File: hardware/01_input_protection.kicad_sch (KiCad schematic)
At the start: 22 parts, among them J1 USB4105-GF-A, Q1 MMBT3906, U1 CH224K, U2 TPS26600PWPR

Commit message: Update on the PCB.
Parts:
- U1: value CH224K -> CH224A

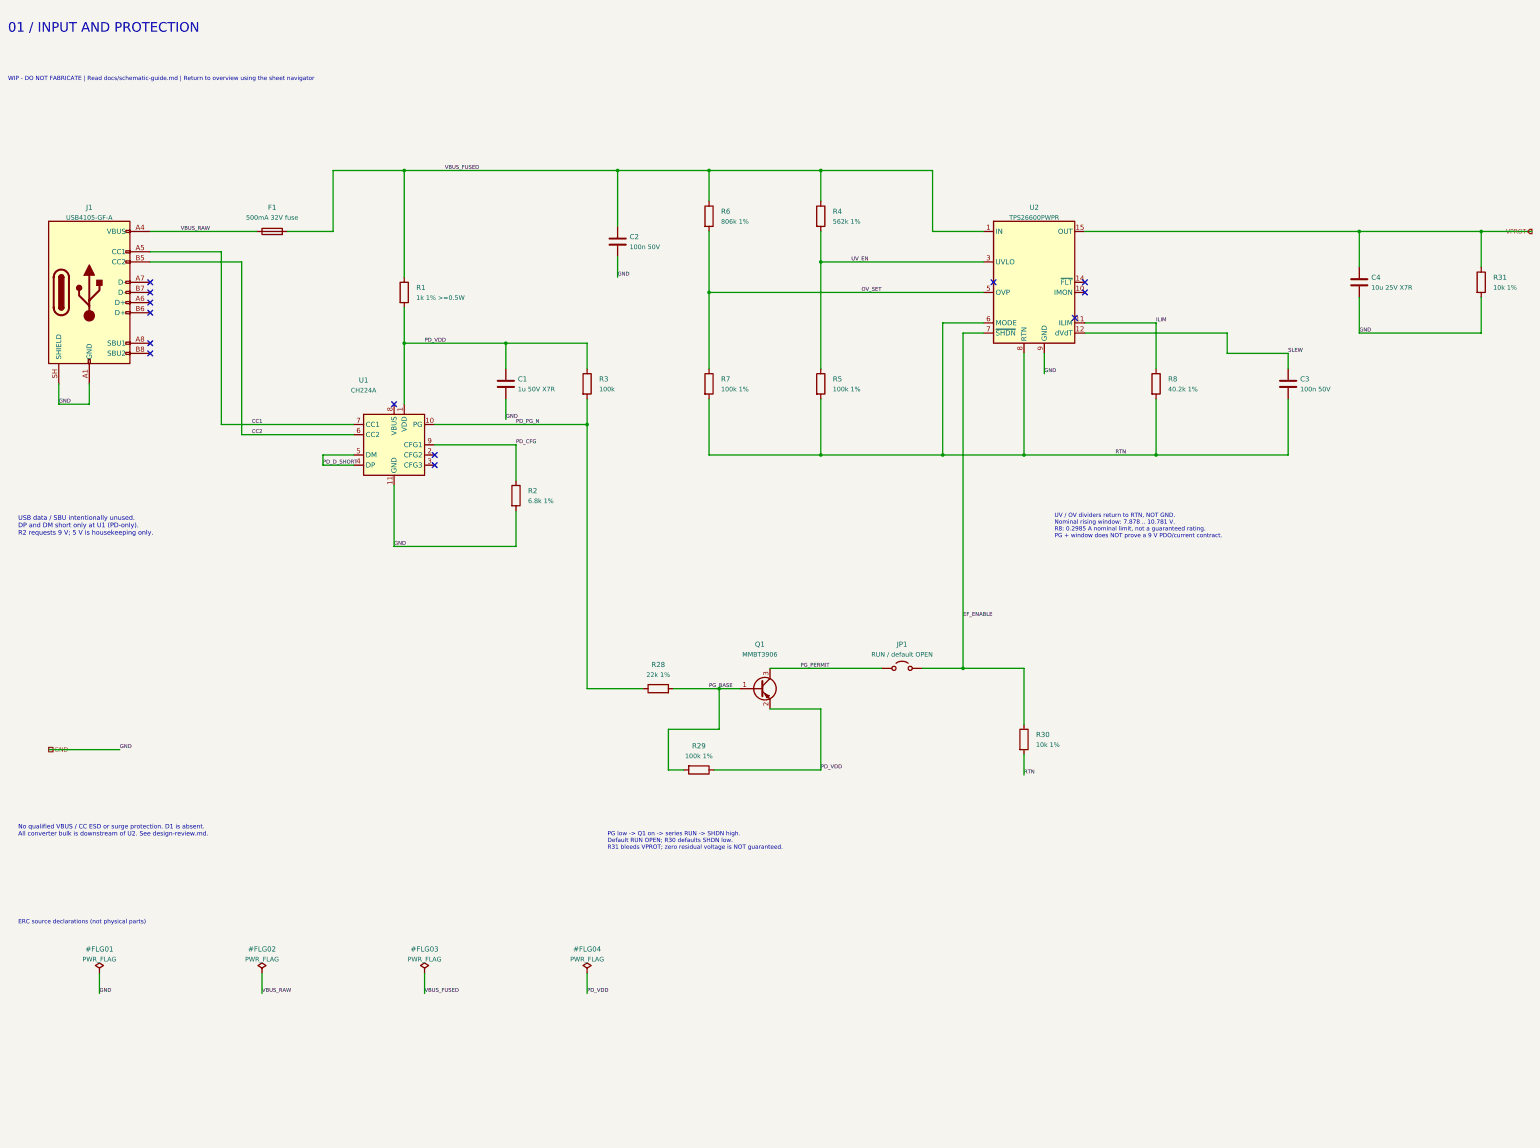
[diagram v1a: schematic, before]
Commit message: Save 9 V power-supply schematic prototype and LED mechanical provisions
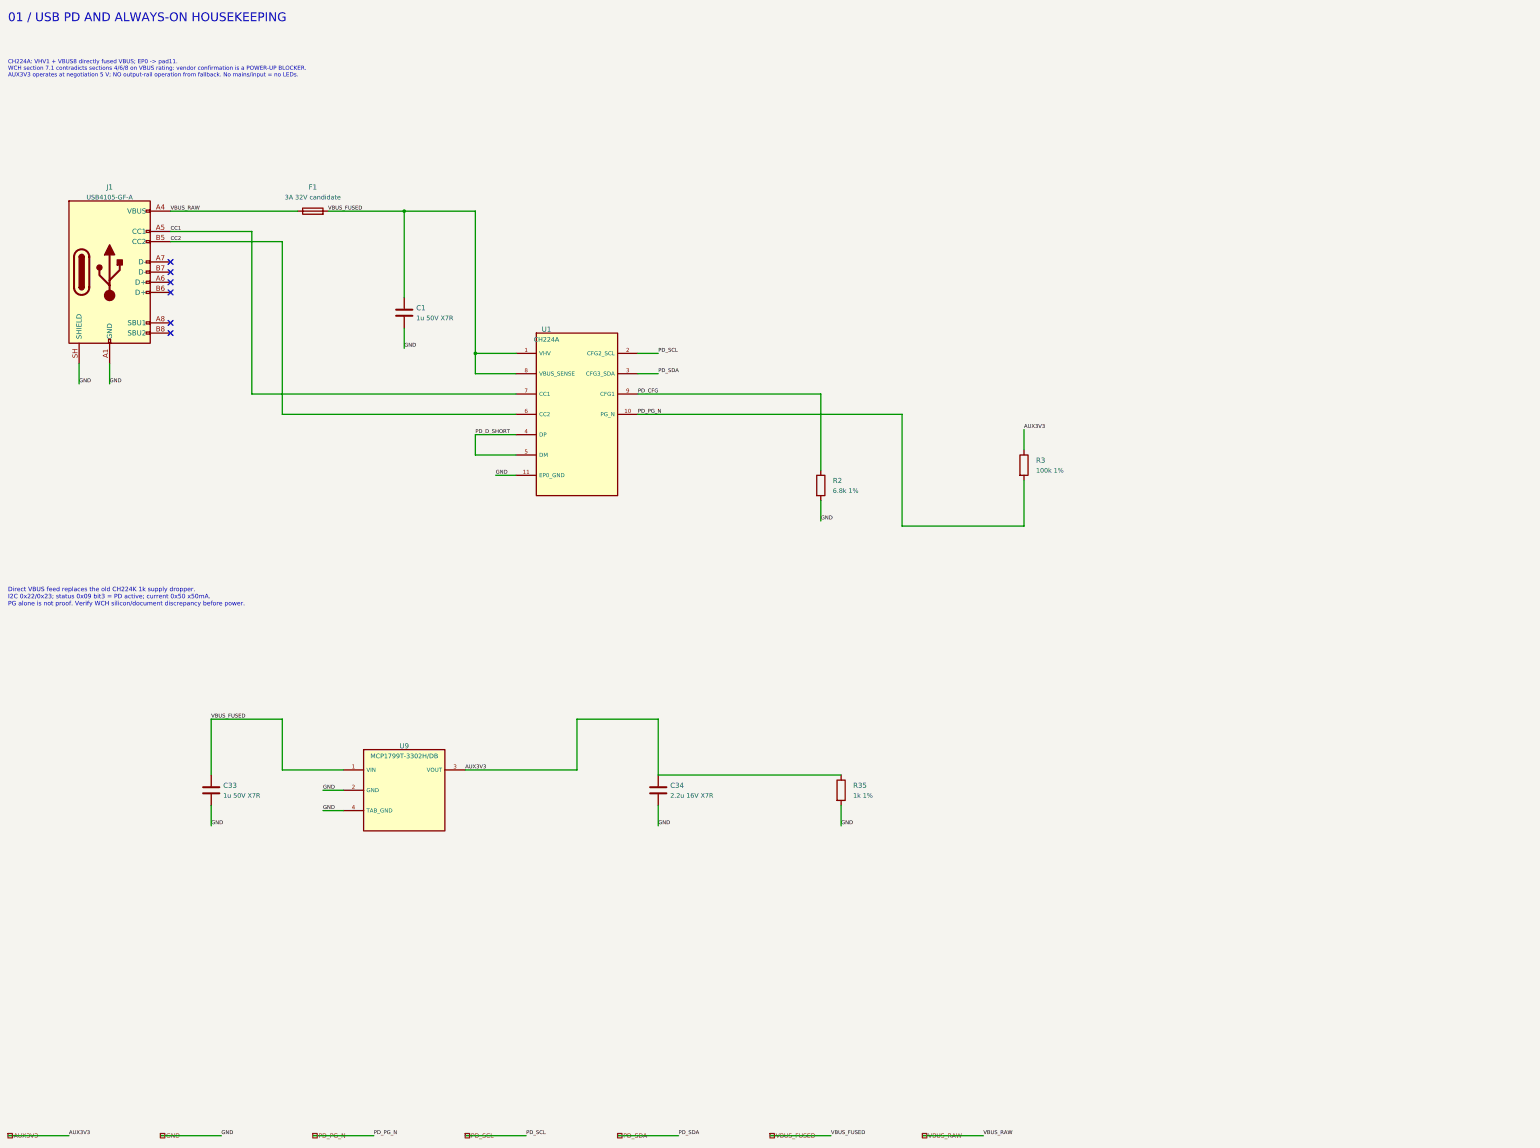
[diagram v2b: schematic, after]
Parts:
- removed C2, C3: 100n 50V, Capacitor_SMD:C_1206_3216Metric, symbol BigModular:Device_C
- removed C4: 10u 25V X7R, Capacitor_SMD:C_1206_3216Metric, symbol BigModular:Device_C
- removed JP1: RUN / default OPEN, symbol BigModular:Jumper_Jumper_2_Open
- removed Q1: MMBT3906, Package_TO_SOT_SMD:SOT-23, symbol BigModular:Transistor_BJT_MMBT3906
- removed R1: 1k 1% >=0.5W, Resistor_SMD:R_2010_5025Metric, symbol BigModular:Device_R
- removed R28: 22k 1%, Resistor_SMD:R_0603_1608Metric, symbol BigModular:Device_R
- removed R29, R5, R7: 100k 1%, Resistor_SMD:R_0603_1608Metric, symbol BigModular:Device_R
- removed R30, R31: 10k 1%, Resistor_SMD:R_0603_1608Metric, symbol BigModular:Device_R
- removed R4: 562k 1%, Resistor_SMD:R_0603_1608Metric, symbol BigModular:Device_R
- removed R6: 806k 1%, Resistor_SMD:R_0603_1608Metric, symbol BigModular:Device_R
- removed R8: 40.2k 1%, Resistor_SMD:R_0603_1608Metric, symbol BigModular:Device_R
- removed U2: TPS26600PWPR, Package_SO:HTSSOP-16-1EP_4.4x5mm_P0.65mm_EP3.4x5mm_Mask2.66x2.46mm_ThermalVias, symbol BigModular:Power_Management_TPS26600PWP
- added C33: 1u 50V X7R, BigModular:C_0805_2012Metric, symbol BigModular:Device_C
- added C34: 2.2u 16V X7R, BigModular:C_0805_2012Metric, symbol BigModular:Device_C
- added R35: 1k 1%, BigModular:R_0603_1608Metric, symbol BigModular:Device_R
- added U9: MCP1799T-3302H/DB, BigModular:MCP1799_SOT223_Tab4, symbol BigModular:MCP1799T_3302H_DB
- C1: footprint Capacitor_SMD:C_1206_3216Metric -> BigModular:C_0805_2012Metric; JLCPCB Audit Requirements (none) -> {}; JLCPCB Exclude (none) -> no; NOTE (none) -> Effective capacitance under DC bias and temperature must be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
- F1: value 500mA 32V fuse -> 3A 32V candidate; footprint (none) -> BigModular:Fuse_1206_3216Metric; JLCPCB Audit Requirements (none) -> {}; JLCPCB Exclude (none) -> no; LCSC (none) -> C14165; MPN (none) -> 0466003.NRHF; NOTE Unselected candidate: 32V rating covers steady 20/21V only;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 -> 0466003.NRHF catalog candidate only; source/fuse/eFuse ther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
- J1: JLCPCB Audit Requirements (none) -> {"assembly": "manual", "reason": "User-selected manual inte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; JLCPCB Exclude (none) -> yes; NOTE Only electrical footprint placed. Drawing Rev B: axis 1.73 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 -> Prototype candidate; qualify ratings, land pattern and oper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
- R2: footprint Resistor_SMD:R_0603_1608Metric -> BigModular:R_0603_1608Metric; JLCPCB Audit Requirements (none) -> {}; JLCPCB Exclude (none) -> no; LCSC (none) -> C23212; MPN (none) -> 0603WAF6801T5E; NOTE (none) -> Prototype candidate; qualify ratings, land pattern and oper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
- R3: value 100k -> 100k 1%; footprint Resistor_SMD:R_0603_1608Metric -> BigModular:R_0603_1608Metric; JLCPCB Audit Requirements (none) -> {}; JLCPCB Exclude (none) -> no; LCSC (none) -> C25803; MPN (none) -> 0603WAF1003T5E; NOTE (none) -> Prototype candidate; qualify ratings, land pattern and oper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
- U1: footprint Package_SO:SSOP-10-1EP_3.9x4.9mm_P1mm_EP2.1x3.3mm -> BigModular:SSOP-10-1EP_3.9x4.9mm_P1mm_EP2.1x3.3mm; symbol BigModular:Interface_USB_CH224K -> BigModular:CH224A; JLCPCB Audit Requirements (none) -> {}; JLCPCB Exclude (none) -> no; LCSC C970725 -> C42459160; MPN CH224K -> CH224A; NOTE WCH v1F fig6.1/6.3; datasheet EP0 maps to library pad11. DP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 -> WCH V2 table4-1; VHV1 is high-voltage input. EP0 mapped to 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
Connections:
- net GND: now also C33.2, C34.2, R35.2, U9.2 (GND), U9.4 (TAB_GND)
- net VBUS_FUSED: now also C1.1, U1.1 (VHV), U1.8 (VBUS_SENSE), C33.1, U9.1 (VIN)
- net PD_SCL: now reaches U1.2 (CFG2_SCL)
- net PD_SDA: now reaches U1.3 (CFG3_SDA)
- removed net PD_VDD: C1.1, R3.1, U1.1 (VDD)
- new net AUX3V3: C34.1, R3.1, R35.1, U9.3 (VOUT)
- no-connect marks 13 -> 6
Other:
- note added: "01 / USB PD AND ALWAYS-ON HOUSEKEEPING"
- note added: "CH224A: VHV1 + VBUS8 directly fused VBUS; EP0 -> pad11. WCH section 7.1 contradicts sections 4/6/8 on VBUS rating: vendor confirmation is a POWER-UP BLOCKER. AUX3V3 operates at negotiation 5 V; NO output-rail operation from fallback. No mains/input = no LEDs."
- note added: "Direct VBUS feed replaces the old CH224K 1k supply dropper. I2C 0x22/0x23; status 0x09 bit3 = PD active; current 0x50 x50mA. PG alone is not proof. Verify WCH silicon/document discrepancy before power."
- note removed: "01 / INPUT AND PROTECTION"
- note removed: "ERC source declarations (not physical parts)"
- note removed: "No qualified VBUS / CC ESD or surge protection. D1 is absent. All converter bulk is downstream of U2. See design-review.md."
- note removed: "PG low -> Q1 on -> series RUN -> SHDN high. Default RUN OPEN; R30 defaults SHDN low. R31 bleeds VPROT; zero residual voltage is NOT guaranteed."
- note removed: "USB data / SBU intentionally unused. DP and DM short only at U1 (PD-only). R2 requests 9 V; 5 V is housekeeping only."
- note removed: "UV / OV dividers return to RTN, NOT GND. Nominal rising window: 7.878 .. 10.781 V. R8: 0.2985 A nominal limit, not a guaranteed rating. PG + window does NOT prove a 9 V PDO/current contract."
- note removed: "WIP - DO NOT FABRICATE | Read docs/schematic-guide.md | Return to overview using the sheet navigator"
- title: Big Modular - Input and protection -> Big Modular - USB PD and always-on housekeeping
- moved on the sheet: C1, F1, J1, R2, R3, U1

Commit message: Clarify hierarchical ports and replace local label islands with visible schematic wiring
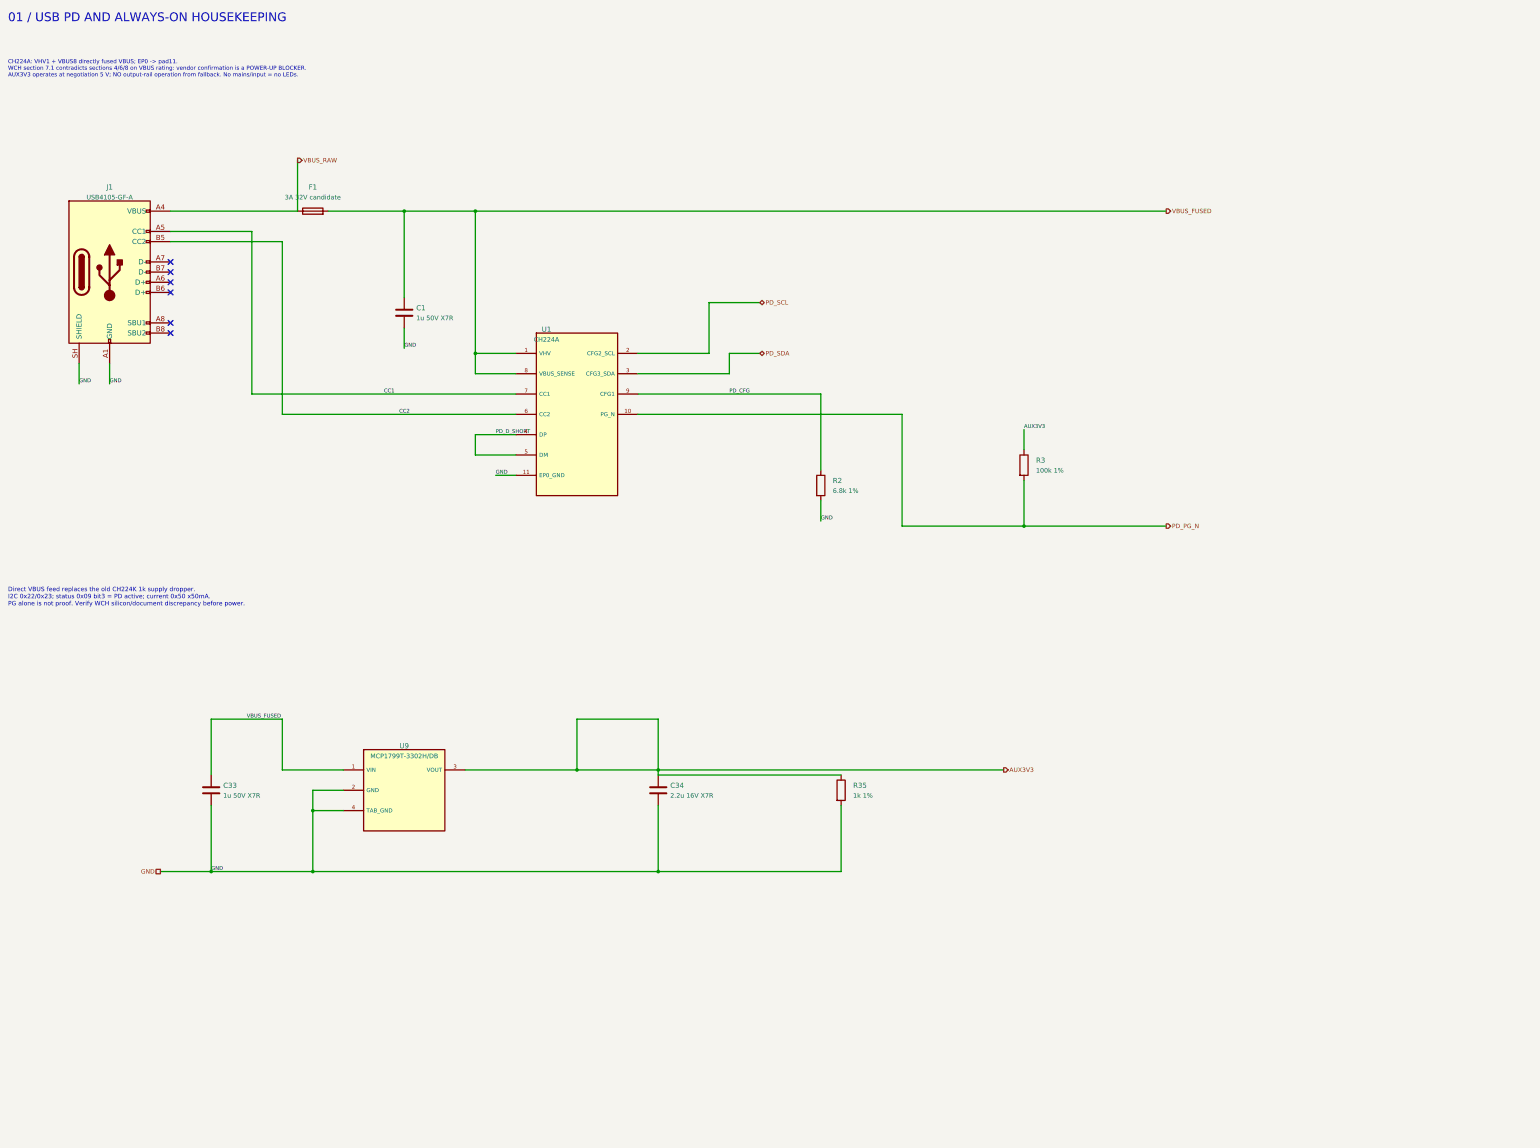
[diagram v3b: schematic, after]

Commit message: Simplify V1 power architecture, remove auxiliary sensing and obsolete documentation, enable autonomous protected start and reset button
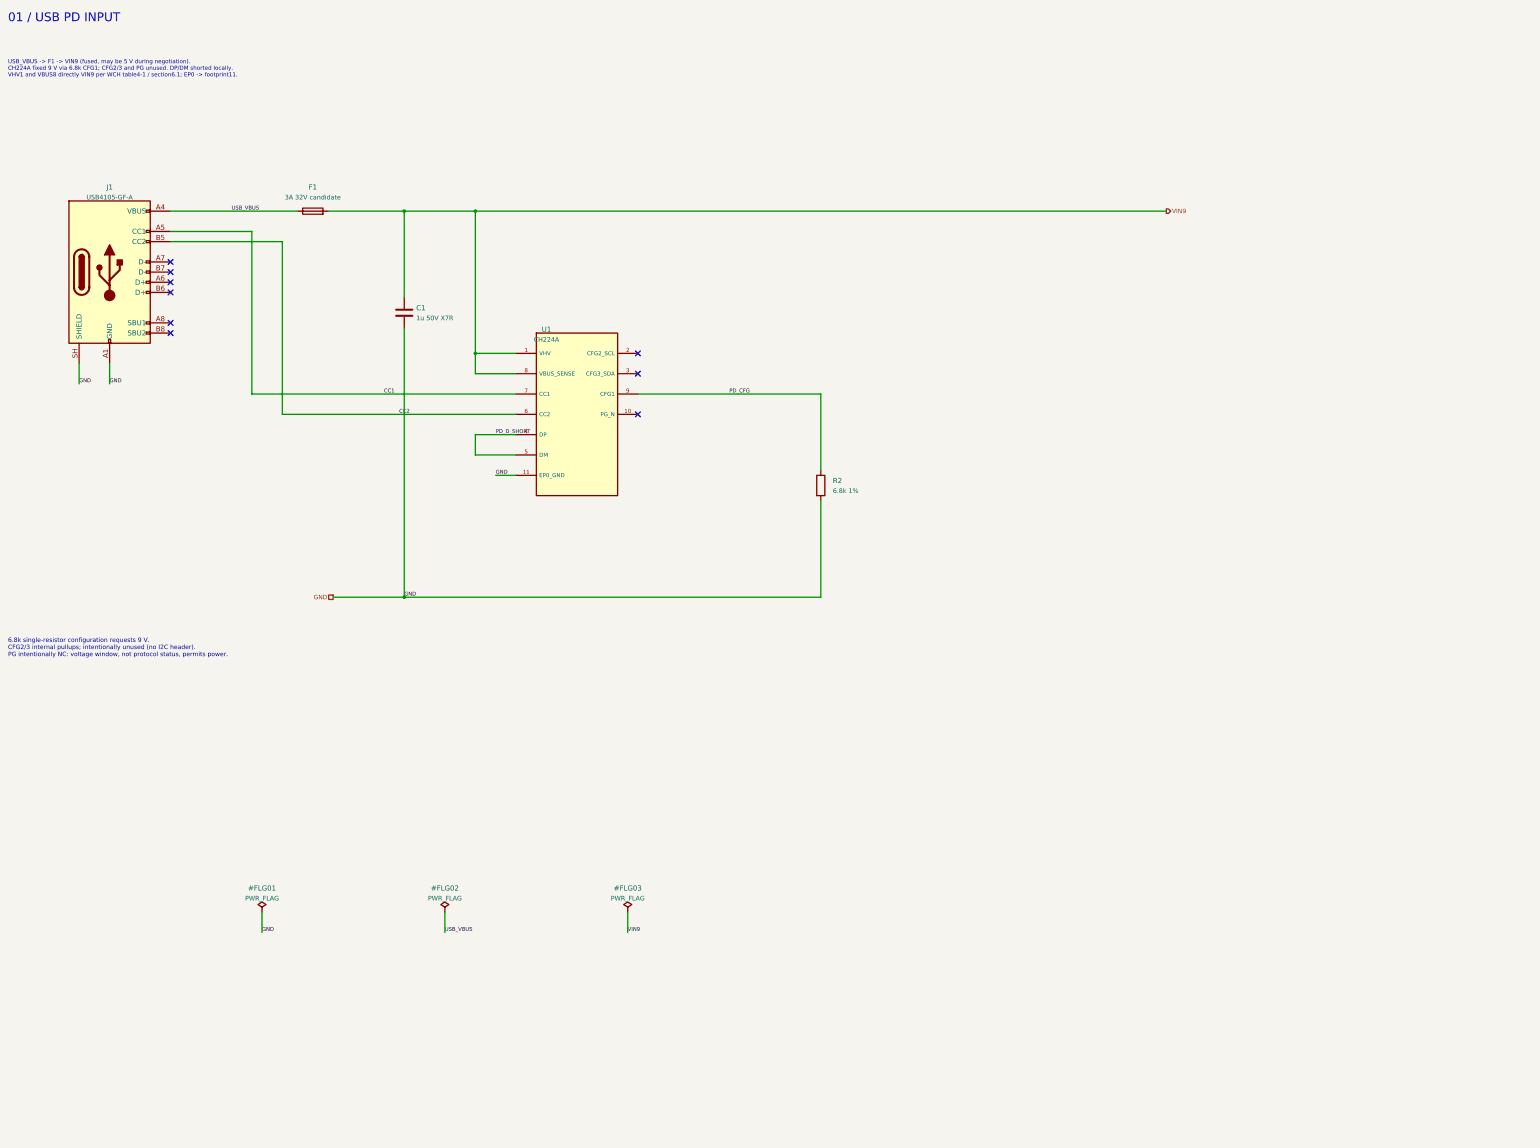
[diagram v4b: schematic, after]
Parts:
- removed C33: 1u 50V X7R, BigModular:C_0805_2012Metric, symbol BigModular:Device_C
- removed C34: 2.2u 16V X7R, BigModular:C_0805_2012Metric, symbol BigModular:Device_C
- removed R3: 100k 1%, BigModular:R_0603_1608Metric, symbol BigModular:Device_R
- removed R35: 1k 1%, BigModular:R_0603_1608Metric, symbol BigModular:Device_R
- removed U9: MCP1799T-3302H/DB, BigModular:MCP1799_SOT223_Tab4, symbol BigModular:MCP1799T_3302H_DB
- U1: NOTE WCH V2 table4-1; VHV1 is high-voltage input. EP0 mapped to pad11. Section7.1 VBUS contradiction unresolved. -> WCH V2 table4-1; VHV1 is high-voltage input. EP0 mapped to pad11. Section7.1 typo resolved against pin table4-1, app6.1 and rating8.1.1; see engineering note.
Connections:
- net PD_PG_N: no longer names the net of U1.10 (PG_N)
- net PD_SCL: no longer names the net of U1.2 (CFG2_SCL)
- net PD_SDA: no longer names the net of U1.3 (CFG3_SDA)
- net VBUS_FUSED renamed VIN9
- net VBUS_RAW renamed USB_VBUS
- no-connect marks 6 -> 9
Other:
- note added: "01 / USB PD INPUT"
- note added: "6.8k single-resistor configuration requests 9 V. CFG2/3 internal pullups; intentionally unused (no I2C header). PG intentionally NC: voltage window, not protocol status, permits power."
- note added: "USB_VBUS -> F1 -> VIN9 (fused, may be 5 V during negotiation). CH224A fixed 9 V via 6.8k CFG1; CFG2/3 and PG unused. DP/DM shorted locally. VHV1 and VBUS8 directly VIN9 per WCH table4-1 / section6.1; EP0 -> footprint11."
- note removed: "01 / USB PD AND ALWAYS-ON HOUSEKEEPING"
- note removed: "CH224A: VHV1 + VBUS8 directly fused VBUS; EP0 -> pad11. WCH section 7.1 contradicts sections 4/6/8 on VBUS rating: vendor confirmation is a POWER-UP BLOCKER. AUX3V3 operates at negotiation 5 V; NO output-rail operation from fallback. No mains/input = no LEDs."
- note removed: "Direct VBUS feed replaces the old CH224K 1k supply dropper. I2C 0x22/0x23; status 0x09 bit3 = PD active; current 0x50 x50mA. PG alone is not proof. Verify WCH silicon/document discrepancy before power."
- title: Big Modular - USB PD and always-on housekeeping -> Big Modular - USB PD input
